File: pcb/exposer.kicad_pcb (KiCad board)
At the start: 2 copper layers, 10 parts, among them IC1 ULN2065B, J1 Conn_01x04_Female, J2 Conn_01x02, SW1 SW_Push, SW2 SW_Push, SW3 SW_Push, SW4 SW_SPST

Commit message: encoder pcb
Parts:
- removed IC1: ULN2065B, Package_DIP:DIP-16_W7.62mm_LongPads
- removed SW2, SW3: SW_Push, Button_Switch_THT:SW_PUSH_6mm_H5mm
- added U2: ULN2003A, Package_DIP:DIP-16_W7.62mm_LongPads, F.Cu at (29.8, 75.9)
- BT1: footprint Battery:BatteryHolder_Keystone_1042_1x18650 -> Battery:BatteryHolder_MPD_BH-18650-PC; moved to F.Cu
- J2: footprint Connector_Wire:SolderWirePad_1x02_P7.62mm_Drill2mm -> Connector_Wire:SolderWire-0.75sqmm_1x02_P4.8mm_D1.25mm_OD2.3mm
- SW1: value SW_Push -> RotaryEncoder_Switch; footprint Button_Switch_THT:SW_PUSH_6mm_H5mm -> Rotary_Encoder:RotaryEncoder_Alps_EC11E-Switch_Vertical_H20mm
- SW4: footprint Connector_Molex:Molex_Micro-Fit_3.0_43650-0315_1x03_P3.00mm_Vertical -> Button_Switch_THT:SW_Slide_SPDT_Straight_CK_OS102011MS2Q
- moved SW1 68.5 mm to (88.9, 62.0), turned to -90 degrees
- moved BT1 49.4 mm to (18.6, 26.5)
- moved A1 40.0 mm to (54.0, 55.6), turned to 90 degrees
- moved U1 31.5 mm to (38.0, 45.0), turned to 0 degrees
- moved J1 18.0 mm to (73.0, 66.0), turned to 0 degrees
- moved J2 13.1 mm to (17.0, 64.3), turned to 90 degrees
- moved SW4 6.31 mm to (19.2, 43.0)
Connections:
- J2 pad 1: +12V -> Net-(J2-Pin_1)
- J2 pad 2: Net-(IC1-O1) -> +12V
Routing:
- net Net-(A1-D4): track 103.9 -> 17.4 mm
- net Net-(A1-D5): track 100.2 -> 19.8 mm
- net +12V: track 121.2 -> 44.9 mm
- net Net-(A1-D6): track 96.7 -> 34.9 mm
- net Net-(IC1-O1): track 55.6 -> 0.00 mm
- net +BATT: track 61.4 -> 11.5 mm
- net +5V: track 56.4 -> 95.8 mm
- net Net-(J2-Pin_1): track 0.00 -> 33.0 mm
- net GND: track 380.0 -> 354.5 mm
- net Net-(A1-D3): track 16.2 -> 30.7 mm
- net Net-(BT1-+): track 9.47 -> 20.3 mm
- net Net-(A1-D2): track 16.2 -> 23.7 mm
- net Net-(A1-D7): track 92.0 -> 88.0 mm
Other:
- board outline added: 83 x 69 mm
- board text removed: "+"
- board text removed: "-"

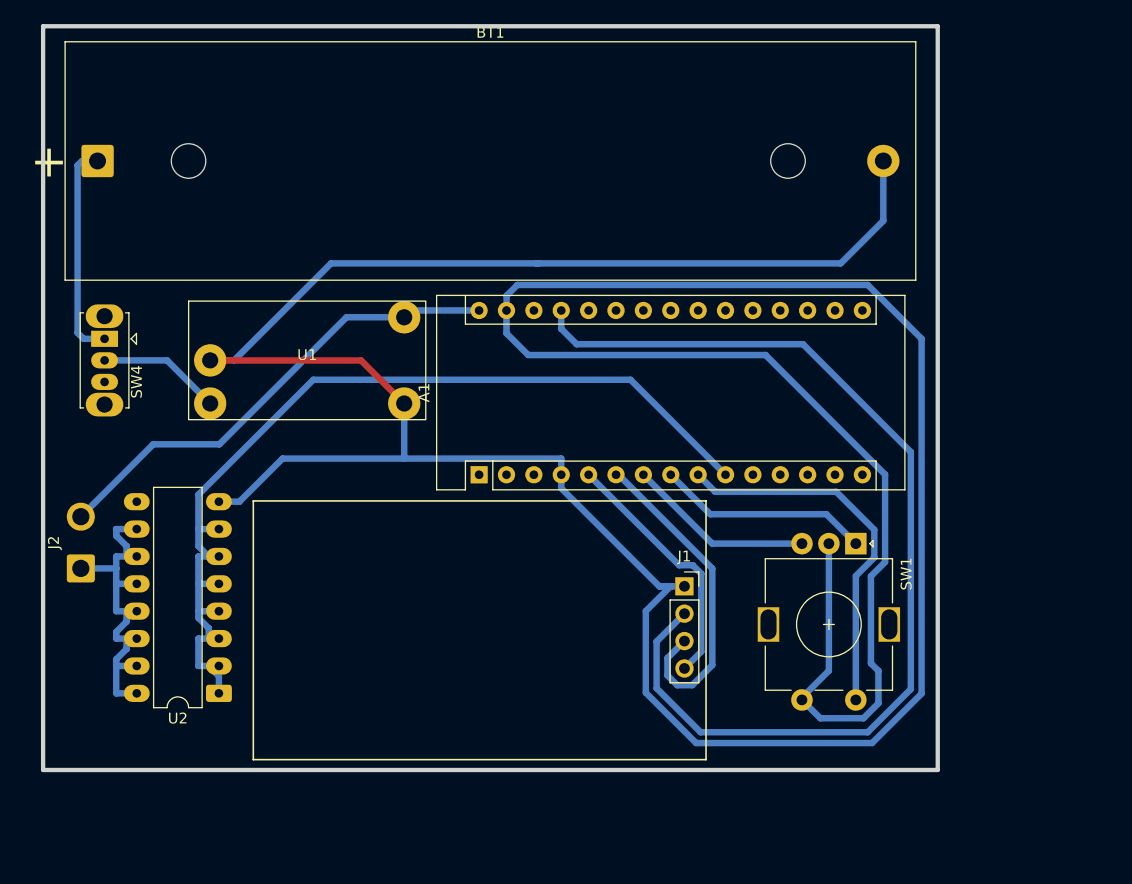
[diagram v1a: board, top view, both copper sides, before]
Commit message: screen was upside down
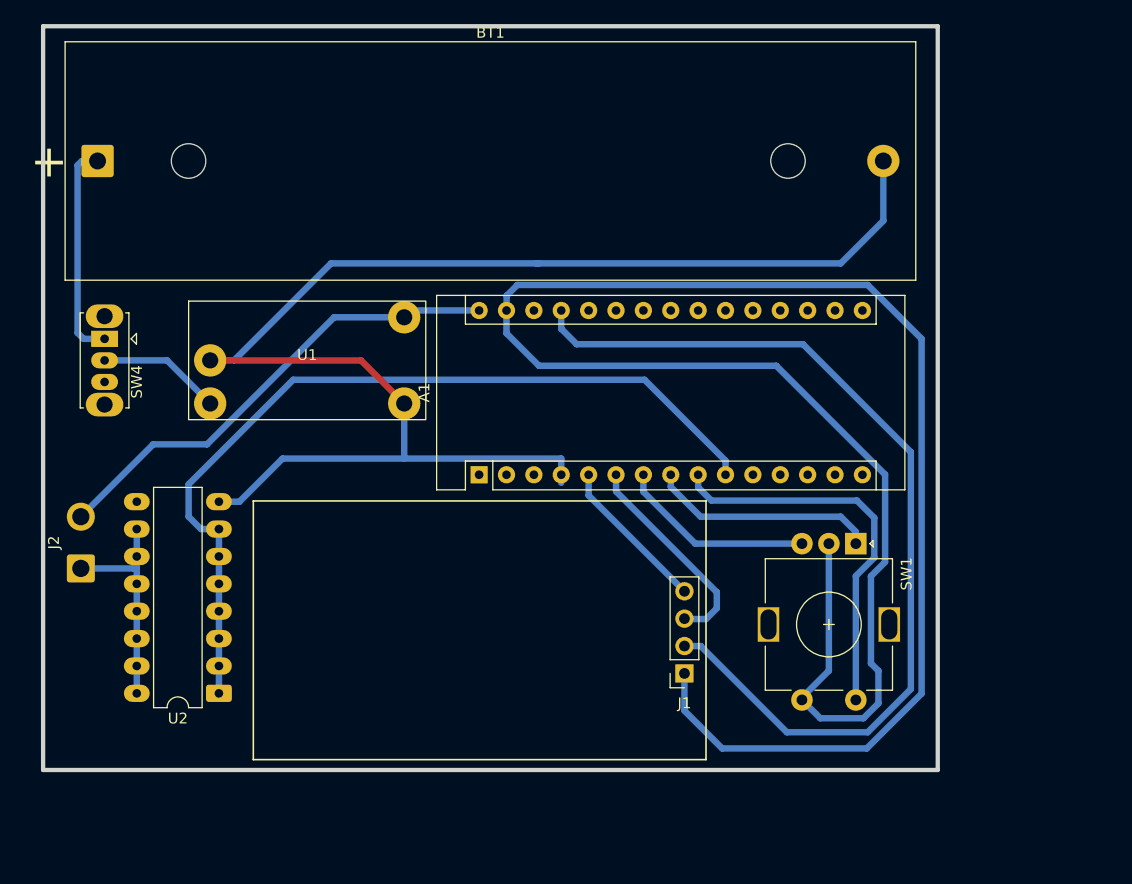
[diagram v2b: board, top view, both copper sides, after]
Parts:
- moved J1 8.08 mm to (73.0, 74.0), turned to 180 degrees
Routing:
- net GND: track 354.5 -> 327.6 mm
- net Net-(J2-Pin_1): track 33.0 -> 20.6 mm
- net Net-(A1-D3): track 30.7 -> 19.9 mm
- net Net-(A1-D2): track 23.7 -> 14.5 mm
- net +5V: track 95.8 -> 86.8 mm
- net Net-(A1-D7): track 88.0 -> 79.8 mm
- net Net-(A1-D6): track 34.9 -> 36.3 mm
- net Net-(A1-D5): track 19.8 -> 21.1 mm
- net Net-(A1-D4): track 17.4 -> 18.3 mm
